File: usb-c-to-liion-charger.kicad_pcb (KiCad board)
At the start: 2 copper layers, 73 parts, among them J1 USB_C_Receptacle_USB2.0, J2 BatteryConnection, Q1 RSJ250P10, Q2 RSJ250P10, Q3 BSC016N06NS, Q4 BSC016N06NS, SW1 SW_DPDT_x2, SW2 SW_SPDT, U1 IP2721, U2 LTC4000-QFN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

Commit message: Finish PCB
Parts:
- C1, R1, R2, R3, U1: moved to B.Cu
- moved H4 130.7 mm to (191.5, 86.5)
- moved H2 117.2 mm to (191.5, 118.0)
- moved H3 105.7 mm to (101.5, 87.0)
- moved J2 84.5 mm to (191.3, 99.8), turned to -90 degrees
- moved R12 83.1 mm to (117.0, 117.5), turned to 90 degrees
- moved R18 81.0 mm to (117.0, 114.2), turned to 90 degrees
- moved R11 79.3 mm to (120.5, 117.5), turned to 90 degrees
- moved F1 77.9 mm to (110.6, 102.2), turned to 90 degrees
- moved J1 77.9 mm to (101.8, 102.2)
- moved R17 77.5 mm to (120.5, 114.2), turned to 90 degrees
- moved F2 77.0 mm to (184.0, 102.2), turned to 90 degrees
- moved C1 76.7 mm to (115.9, 107.8), turned to 180 degrees
- moved H1 74.9 mm to (101.5, 118.0)
- moved R1 73.7 mm to (116.7, 98.4), turned to -90 degrees
- moved R10 73.5 mm to (118.8, 117.5), turned to 90 degrees
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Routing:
- net /Charge-IC/BAT: track 0.00 -> 101.5 mm, vias 0 -> 2
- net /Boost-Converter/INTV_{CC}: track 26.0 -> 93.1 mm, vias 2 -> 3
- net Net-(C7-Pad1): track 0.00 -> 66.2 mm, vias 0 -> 2
- net Net-(C2-Pad1): track 0.00 -> 61.2 mm
- net Net-(R14-Pad3): track 0.00 -> 57.7 mm
- net /Charge-IC/CSP: track 0.00 -> 53.9 mm, vias 0 -> 4
- net Net-(Q1-Pad1): track 0.00 -> 53.5 mm
- net /Charge-IC/OFB: track 0.00 -> 34.2 mm, vias 0 -> 2
- net /Charge-IC/~{FAULT}: track 0.00 -> 31.0 mm, vias 0 -> 2
- net /Charge-IC/FBG: track 0.00 -> 28.9 mm
- net /Charge-IC/~{CHARGE}: track 0.00 -> 27.8 mm, vias 0 -> 2
- net /Charge-IC/BIAS: track 0.00 -> 27.1 mm, vias 0 -> 2
- net /Boost-Converter/SS: track 5.47 -> 30.5 mm, vias 0 -> 3
- net /Boost-Converter/ITH: track 3.45 -> 25.8 mm
- net /Charge-IC/BFB: track 0.00 -> 20.1 mm
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- added copper zone on F.Cu, net /Charge-IC/CSP
- added copper zone on F.Cu, net /Charge-IC/VIN
- added copper zone on B.Cu, net GND
- added copper zone on F.Cu, net GND
- added copper zone on B.Cu, net Net-(C18-Pad1)
- added copper zone on F.Cu, net Net-(Q2-Pad3)
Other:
- board outline added: 98 x 39.5 mm
- board text added: "USB-C to Li-Ion charger v1.0 2022-05 by MG"

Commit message: Optimize ground vias
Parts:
- moved R8 0.25 mm to (157.5, 114.5)
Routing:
- net /Boost-Converter/V_{OUT}: track 7.80 -> 15.3 mm
- net /Charge-IC/FBG: track 28.9 -> 23.5 mm
- net GND: track 12.1 -> 14.4 mm, vias 78 -> 116
- net Net-(Q1-Pad1): track 53.5 -> 51.5 mm
- net Net-(C12-Pad2): track 16.4 -> 17.5 mm
- net Net-(C7-Pad1): track 66.2 -> 67.1 mm
- net /Charge-IC/OFB: track 34.2 -> 33.5 mm
- net /Charge-IC/CSP: track 53.9 -> 54.6 mm
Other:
- board text added: "USB-C PD to 10S/12S Li-Ion charger v1.0 2022-05 by MG"
- board text removed: "USB-C to Li-Ion charger v1.0 2022-05 by MG"

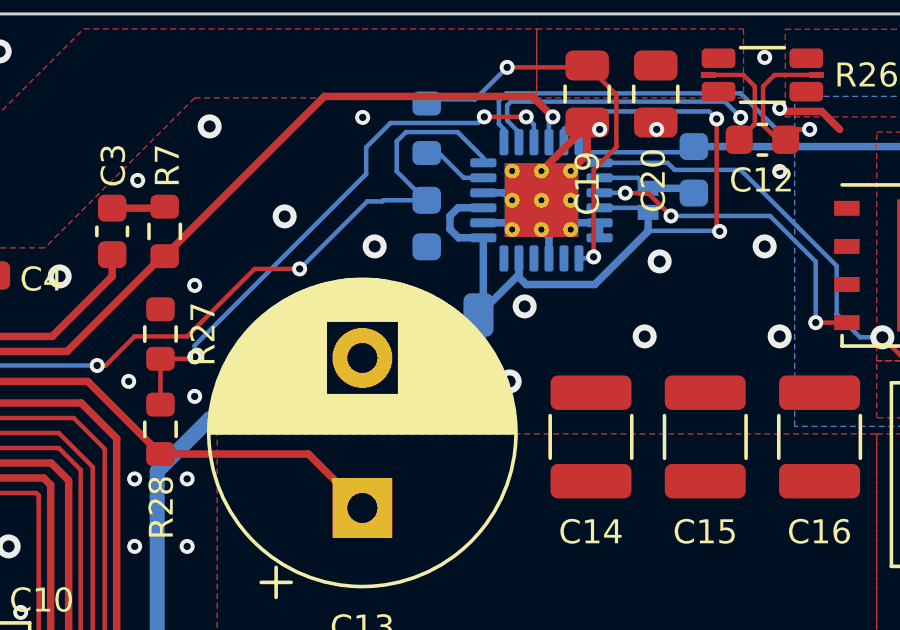
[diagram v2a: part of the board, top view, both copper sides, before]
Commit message: Update BOM due component order
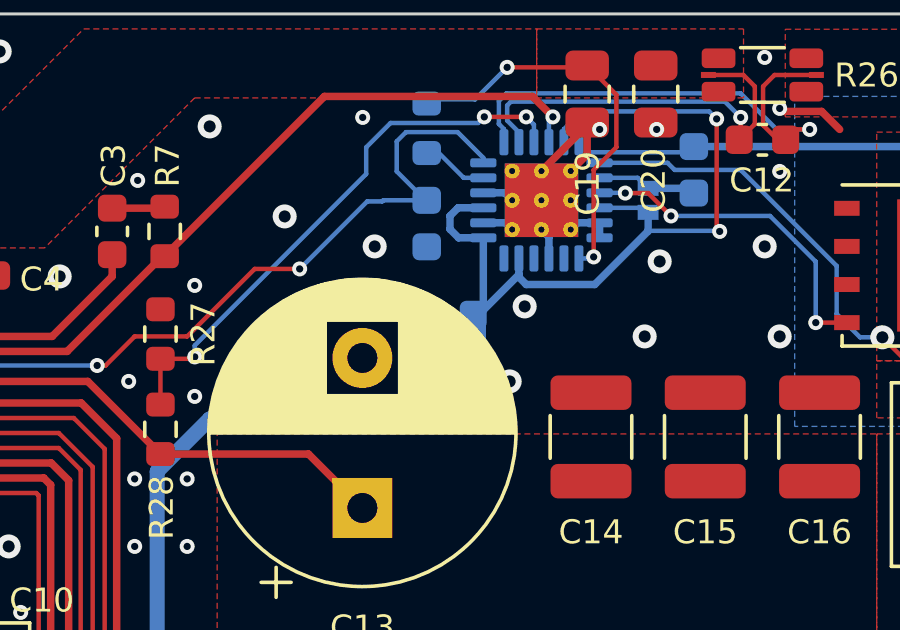
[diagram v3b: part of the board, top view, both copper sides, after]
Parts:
- C22: footprint Capacitor_SMD:C_0805_2012Metric -> Capacitor_SMD:C_0603_1608Metric
- R21, R22: value 6k -> 6k8
- R23: value 6k5 -> 6k49
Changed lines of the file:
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@@
       (effects (font (size 0.8 0.8) (thickness 0.1)))
     )
-    (fp_text value "6k" (at 0 1.43 90) (layer "F.Fab")
+    (fp_text value "6k8" (at 0 1.43 90) (layer "F.Fab")
       (effects (font (size 1 1) (thickness 0.15)))
     )
@@
       (effects (font (size 0.8 0.8) (thickness 0.1)))
     )
-    (fp_text value "6k5" (at 0 1.43) (layer "F.Fab")
+    (fp_text value "6k49" (at 0 1.43) (layer "F.Fab")
       (effects (font (size 1 1) (thickness 0.15)))
     )
@@
       (effects (font (size 0.8 0.8) (thickness 0.1)))
     )
-    (fp_text value "6k" (at 0 1.43) (layer "F.Fab")
+    (fp_text value "6k8" (at 0 1.43) (layer "F.Fab")
       (effects (font (size 1 1) (thickness 0.15)))
     )
@@
     )
   )
-  (footprint "Capacitor_SMD:C_0805_2012Metric" (layer "B.Cu")
+  (footprint "Capacitor_SMD:C_0603_1608Metric" (layer "B.Cu")
     (at 146.011 92.536 180)
-    (descr "Capacitor SMD 0805 (2012 Metric), square (rectangular) end terminal, IPC_7351 nominal, (Body size source: IPC-SM-782 page 76, https://www.pcb-3d.com/wordpress/wp-content/uploads/ipc-sm-782a_amendment_1_and_2.pdf, https://docs.google.com/spreadsheets/d/1BsfQQcO9C6DZCsRaXUlFlo91Tg2WpOkGARC1WS5S8t0/edit?usp=sharing), generated with kicad-footprint-generator")
+    (descr "Capacitor SMD 0603 (1608 Metric), square (rectangular) end terminal, IPC_7351 nominal, (Body size source: IPC-SM-782 page 76, https://www.pcb-3d.com/wordpress/wp-content/uploads/ipc-sm-782a_amendment_1_and_2.pdf), generated with kicad-footprint-generator")
     (tags "capacitor")
     (property "Sheetfile" "Boost-Converter.kicad_sch")
     (property "Sheetname" "Boost-Converter")
     (attr smd)
-    (fp_text reference "C22" (at -2.689 -0.014 unlocked) (layer "B.SilkS")
-      (effects (font (size 0.8 0.8) (thickness 0.1)) (justify mirror))
-    )
-    (fp_text value "1uF" (at 0 -1.68) (layer "B.Fab")
+    (fp_text reference "C22" (at 0 1.43) (layer "B.SilkS")
       (effects (font (size 1 1) (thickness 0.15)) (justify mirror))
     )
+    (fp_text value "1uF" (at 0 -1.43) (layer "B.Fab")
+      (effects (font (size 1 1) (thickness 0.15)) (justify mirror))
+    )
     (fp_text user "${REFERENCE}" (at 0 0) (layer "B.Fab")
-      (effects (font (size 0.5 0.5) (thickness 0.08)) (justify mirror))
-    )
-    (fp_line (start -0.261252 0.735) (end 0.261252 0.735) (layer "B.SilkS") (width 0.12))
-    (fp_line (start -0.261252 -0.735) (end 0.261252 -0.735) (layer "B.SilkS") (width 0.12))
-    (fp_line (start -1.7 0.98) (end 1.7 0.98) (layer "B.CrtYd") (width 0.05))
-    (fp_line (start 1.7 -0.98) (end -1.7 -0.98) (layer "B.CrtYd") (width 0.05))
-    (fp_line (start 1.7 0.98) (end 1.7 -0.98) (layer "B.CrtYd") (width 0.05))
-    (fp_line (start -1.7 -0.98) (end -1.7 0.98) (layer "B.CrtYd") (width 0.05))
-    (fp_line (start -1 -0.625) (end -1 0.625) (layer "B.Fab") (width 0.1))
-    (fp_line (start 1 0.625) (end 1 -0.625) (layer "B.Fab") (width 0.1))
-    (fp_line (start 1 -0.625) (end -1 -0.625) (layer "B.Fab") (width 0.1))
-    (fp_line (start -1 0.625) (end 1 0.625) (layer "B.Fab") (width 0.1))
-    (pad "1" smd roundrect (at -0.95 0 180) (size 1 1.45) (layers "B.Cu" "B.Paste" "B.Mask") (roundrect_rratio 0.25)
+      (effects (font (size 0.4 0.4) (thickness 0.06)) (justify mirror))
+    )
+    (fp_line (start -0.14058 -0.51) (end 0.14058 -0.51) (layer "B.SilkS") (width 0.12))
+    (fp_line (start -0.14058 0.51) (end 0.14058 0.51) (layer "B.SilkS") (width 0.12))
+    (fp_line (start -1.48 -0.73) (end -1.48 0.73) (layer "B.CrtYd") (width 0.05))
+    (fp_line (start 1.48 0.73) (end 1.48 -0.73) (layer "B.CrtYd") (width 0.05))
+    (fp_line (start 1.48 -0.73) (end -1.48 -0.73) (layer "B.CrtYd") (width 0.05))
+    (fp_line (start -1.48 0.73) (end 1.48 0.73) (layer "B.CrtYd") (width 0.05))
+    (fp_line (start 0.8 -0.4) (end -0.8 -0.4) (layer "B.Fab") (width 0.1))
+    (fp_line (start -0.8 -0.4) (end -0.8 0.4) (layer "B.Fab") (width 0.1))
+    (fp_line (start 0.8 0.4) (end 0.8 -0.4) (layer "B.Fab") (width 0.1))
+    (fp_line (start -0.8 0.4) (end 0.8 0.4) (layer "B.Fab") (width 0.1))
+    (pad "1" smd roundrect (at -0.775 0 180) (size 0.9 0.95) (layers "B.Cu" "B.Paste" "B.Mask") (roundrect_rratio 0.25)
       (net 19 "/Boost-Converter/INTV_{CC}") (pintype "passive"))
-    (pad "2" smd roundrect (at 0.95 0 180) (size 1 1.45) (layers "B.Cu" "B.Paste" "B.Mask") (roundrect_rratio 0.25)
+    (pad "2" smd roundrect (at 0.775 0 180) (size 0.9 0.95) (layers "B.Cu" "B.Paste" "B.Mask") (roundrect_rratio 0.25)
       (net 2 "GND") (pintype "passive"))
-    (model "${KICAD6_3DMODEL_DIR}/Capacitor_SMD.3dshapes/C_0805_2012Metric.wrl"
-      (offset (xyz 0 0 0))
-      (scale (xyz 1 1 1))
+    (model "${KICAD6_3DMODEL_DIR}/Capacitor_SMD.3dshapes/C_0603_1608Metric.wrl"
+      (offset (xyz 0 0 0))
+      (scale (xyz 1 1 1))
